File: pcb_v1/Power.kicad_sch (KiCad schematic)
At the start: 7 parts, among them J1 Conn_01x02, J2 Conn_01x04, U5 MCP73831-2-OT

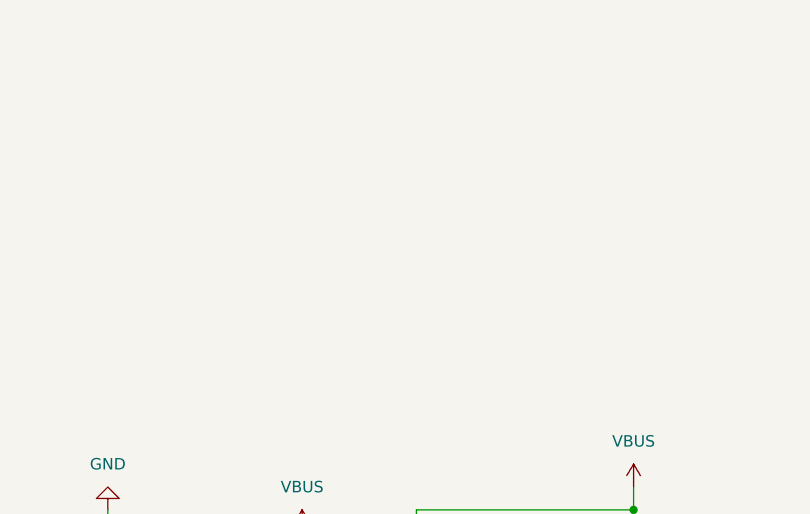
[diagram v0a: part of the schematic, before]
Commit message: New MCU. Added ESP32 S3 Mini1 to act as Bluetooth module
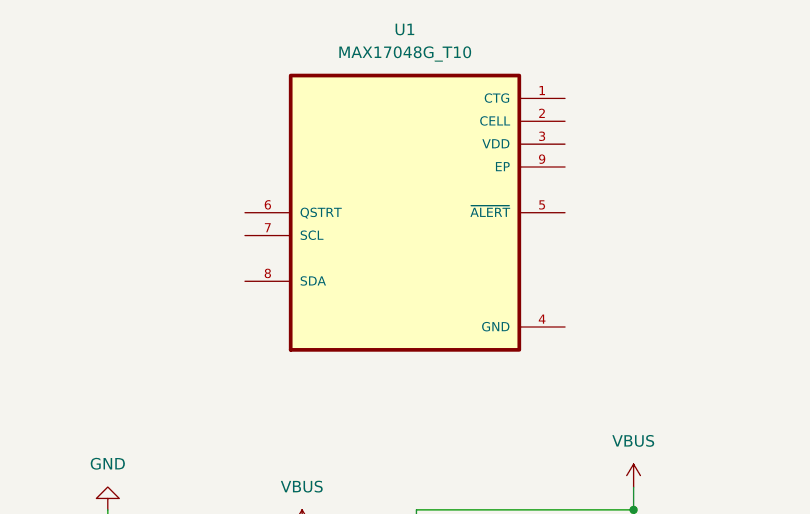
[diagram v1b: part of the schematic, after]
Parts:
- added U1: MAX17048G_T10, MAX17048G_T10:SON50P200X200X80-9N, symbol MAX17048G_T10:MAX17048G_T10
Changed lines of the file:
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@@
+	)
+	(symbol
+		(lib_id "MAX17048G_T10:MAX17048G_T10")
+		(at 125.73 52.07 0)
+		(unit 1)
+		(exclude_from_sim no)
+		(in_bom yes)
+		(on_board yes)
+		(dnp no)
+		(fields_autoplaced yes)
+		(property "Reference" "U1"
+			(at 125.73 31.75 0)
+			(effects
+				(font
+					(size 1.27 1.27)
+				)
+			)
+		)
+		(property "Value" "MAX17048G_T10"
+			(at 125.73 34.29 0)
+			(effects
+				(font
+					(size 1.27 1.27)
+				)
+			)
+		)
+		(property "Footprint" "MAX17048G_T10:SON50P200X200X80-9N"
+			(at 125.73 52.07 0)
+			(effects
+				(font
+					(size 1.27 1.27)
+				)
+				(justify bottom)
+				(hide yes)
+			)
+		)
+		(property "Datasheet" ""
+			(at 125.73 52.07 0)
+			(effects
+				(font
+					(size 1.27 1.27)
+				)
+				(hide yes)
+			)
+		)
+		(property "Description" ""
+			(at 125.73 52.07 0)
+			(effects
+				(font
+					(size 1.27 1.27)
+				)
+				(hide yes)
+			)
+		)
+		(property "MF" "Analog Devices"
+			(at 125.73 52.07 0)
+			(effects
+				(font
+					(size 1.27 1.27)
+				)
+				(justify bottom)
+				(hide yes)
+			)
+		)
+		(property "Description_1" "3µA 1-Cell/2-Cell Fuel Gauge with ModelGauge"
+			(at 125.73 52.07 0)
+			(effects
+				(font
+					(size 1.27 1.27)
+				)
+				(justify bottom)
+				(hide yes)
+			)
+		)
+		(property "Package" "TDFN-8 Maxim"
+			(at 125.73 52.07 0)
+			(effects
+				(font
+					(size 1.27 1.27)
+				)
+				(justify bottom)
+				(hide yes)
+			)
+		)
+		(property "Price" "None"
+			(at 125.73 52.07 0)
+			(effects
+				(font
+					(size 1.27 1.27)
+				)
+				(justify bottom)
+				(hide yes)
+			)
+		)
+		(property "SnapEDA_Link" "https://www.snapeda.com/parts/MAX17048G+T10/Analog+Devices/view-part/?ref=snap"
+			(at 125.73 52.07 0)
+			(effects
+				(font
+					(size 1.27 1.27)
+				)
+				(justify bottom)
+				(hide yes)
+			)
+		)
+		(property "MP" "MAX17048G+T10"
+			(at 125.73 52.07 0)
+			(effects
+				(font
+					(size 1.27 1.27)
+				)
+				(justify bottom)
+				(hide yes)
+			)
+		)
+		(property "Availability" "In Stock"
+			(at 125.73 52.07 0)
+			(effects
+				(font
+					(size 1.27 1.27)
+				)
+				(justify bottom)
+				(hide yes)
+			)
+		)
+		(property "Check_prices" "https://www.snapeda.com/parts/MAX17048G+T10/Analog+Devices/view-part/?ref=eda"
+			(at 125.73 52.07 0)
+			(effects
+				(font
+					(size 1.27 1.27)
+				)
+				(justify bottom)
+				(hide yes)
+			)
+		)
+		(pin "3"
+		)
+		(pin "9"
+		)
+		(pin "4"
+		)
+		(pin "2"
+		)
+		(pin "1"
+		)
+		(pin "6"
+		)
+		(pin "7"
+		)
+		(pin "5"
+		)
+		(pin "8"
+		)
+		(instances
+			(project ""
+				(path "/bf36a815-88b9-4f95-84c3-6b01513341e6/fa53453f-f231-4d4e-b453-0aed75af6d09"
+					(reference "U1")
+					(unit 1)
+				)
+			)
+		)
 	)
 	(symbol

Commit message: Updated wiring
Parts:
- C6, C7: footprint (none) -> Murata Capacitor:CAPC1608X90N
- R2, R4: footprint (none) -> Yageo Resistor:RESC1607X60N
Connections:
- net Status: no longer names the net of R2.2, U5.1 (STAT)
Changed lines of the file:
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@@
 		)
 	)
-	(global_label "Status"
+	(global_label "V_Battery"
 		(shape input)
-		(at 161.29 96.52 0)
+		(at 177.8 83.82 90)
 		(fields_autoplaced yes)
 		(effects
@@
 		)
 		(property "Intersheetrefs" "${INTERSHEET_REFS}"
-			(at 170.2622 96.52 0)
+			(at 177.8 72.0658 90)
 			(effects
 				(font
@@
 	(global_label "V_Battery"
 		(shape input)
-		(at 177.8 83.82 90)
+		(at 184.15 95.25 90)
 		(fields_autoplaced yes)
 		(effects
@@
 		)
 		(property "Intersheetrefs" "${INTERSHEET_REFS}"
-			(at 177.8 72.0658 90)
+			(at 184.15 83.4958 90)
 			(effects
 				(font
@@
 	(global_label "V_Battery"
 		(shape input)
-		(at 184.15 95.25 90)
+		(at 205.74 95.25 90)
 		(fields_autoplaced yes)
 		(effects
@@
 		)
 		(property "Intersheetrefs" "${INTERSHEET_REFS}"
-			(at 184.15 83.4958 90)
-			(effects
-				(font
-					(size 1.27 1.27)
-				)
-				(justify left)
-				(hide yes)
-			)
-		)
-	)
-	(global_label "V_Battery"
+			(at 205.74 83.4958 90)
+			(effects
+				(font
+					(size 1.27 1.27)
+				)
+				(justify left)
+				(hide yes)
+			)
+		)
+	)
+	(global_label "D-"
 		(shape input)
-		(at 205.74 95.25 90)
+		(at 92.71 92.71 0)
 		(fields_autoplaced yes)
 		(effects
@@
 		)
 		(property "Intersheetrefs" "${INTERSHEET_REFS}"
-			(at 205.74 83.4958 90)
-			(effects
-				(font
-					(size 1.27 1.27)
-				)
-				(justify left)
-				(hide yes)
-			)
-		)
-	)
-	(global_label "D-"
-		(shape input)
-		(at 92.71 92.71 0)
-		(fields_autoplaced yes)
-		(effects
-			(font
-				(size 1.27 1.27)
-			)
-			(justify left)
-		)
-		(property "Intersheetrefs" "${INTERSHEET_REFS}"
 			(at 98.5376 92.71 0)
 			(effects
@@
 			)
 		)
-		(property "Footprint" ""
+		(property "Footprint" "Murata Capacitor:CAPC1608X90N"
 			(at 115.2652 96.52 0)
 			(effects
@@
 			)
 		)
-		(property "Footprint" ""
+		(property "Footprint" "Yageo Resistor:RESC1607X60N"
 			(at 125.222 97.79 90)
 			(effects
@@
 			)
 		)
-		(property "Footprint" ""
+		(property "Footprint" "Murata Capacitor:CAPC1608X90N"
 			(at 185.1152 104.14 0)
 			(effects
@@
 			)
 		)
-		(property "Footprint" ""
+		(property "Footprint" "Yageo Resistor:RESC1607X60N"
 			(at 134.112 100.33 90)
 			(effects

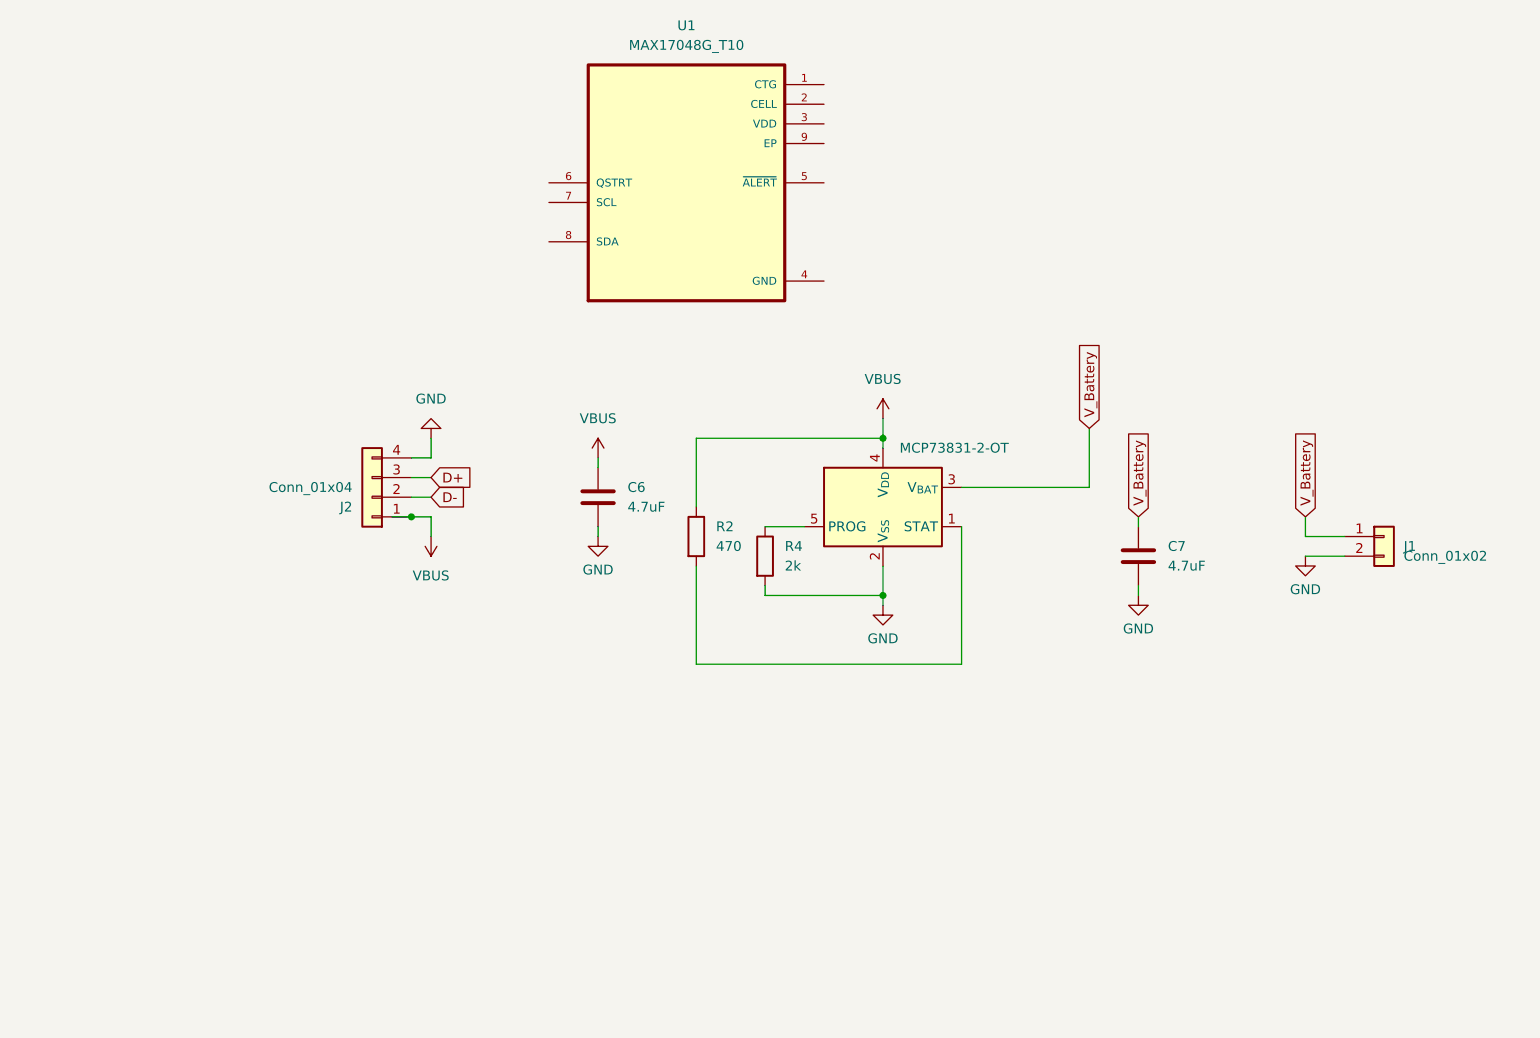
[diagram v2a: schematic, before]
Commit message: Connected OLED pin connector
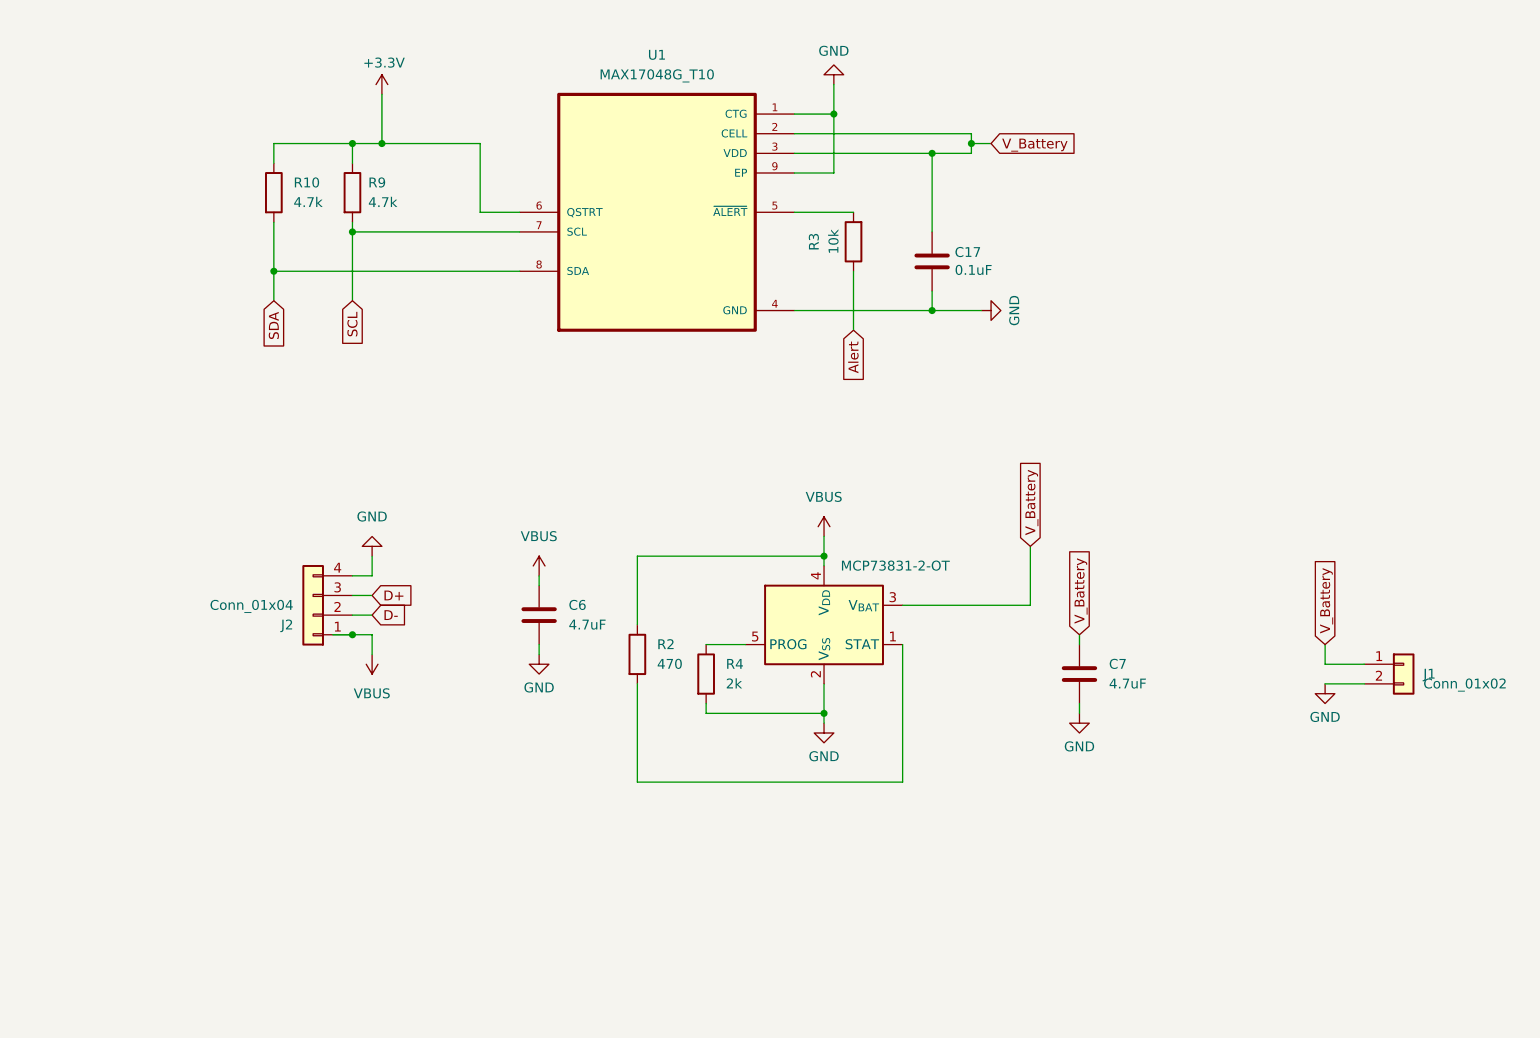
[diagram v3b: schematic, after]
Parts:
- added C17: 0.1uF, GRM1555C2A101GA01D:CAPC1005X55N, symbol Device:C
- added R10, R9: 4.7k, RC0402FR-7D4K7L:RESC1005X40N, symbol Device:R
- added R3: 10k, RC0402FR-7D4K7L:RESC1005X40N, symbol ScottoKeebs:Placeholder_Resistor
- C6, C7: footprint Murata Capacitor:CAPC1608X90N -> GRM1555C2A101GA01D:CAPC1005X55N
- R2, R4: footprint Yageo Resistor:RESC1607X60N -> RC0402FR-7D4K7L:RESC1005X40N
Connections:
- net GND: now also U1.1 (CTG), U1.4 (GND), U1.9 (EP), C17.2
- net V_Battery: now also U1.2 (CELL), U1.3 (VDD), C17.1
- net at U1.5 (~{ALERT}): now also R3.2
- net +3.3V: now reaches U1.6 (QSTRT)
- net +3.3V: now also R10.1, R9.1
- net SCL: now reaches U1.7 (SCL)
- net SCL: now also R9.2
- net SDA: now reaches U1.8 (SDA)
- net SDA: now also R10.2
- new net Alert: R3.1
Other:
- moved on the sheet: C6, C7, J1, J2, R2, R4, U1

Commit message: New Charger IC, Added Ground Plane
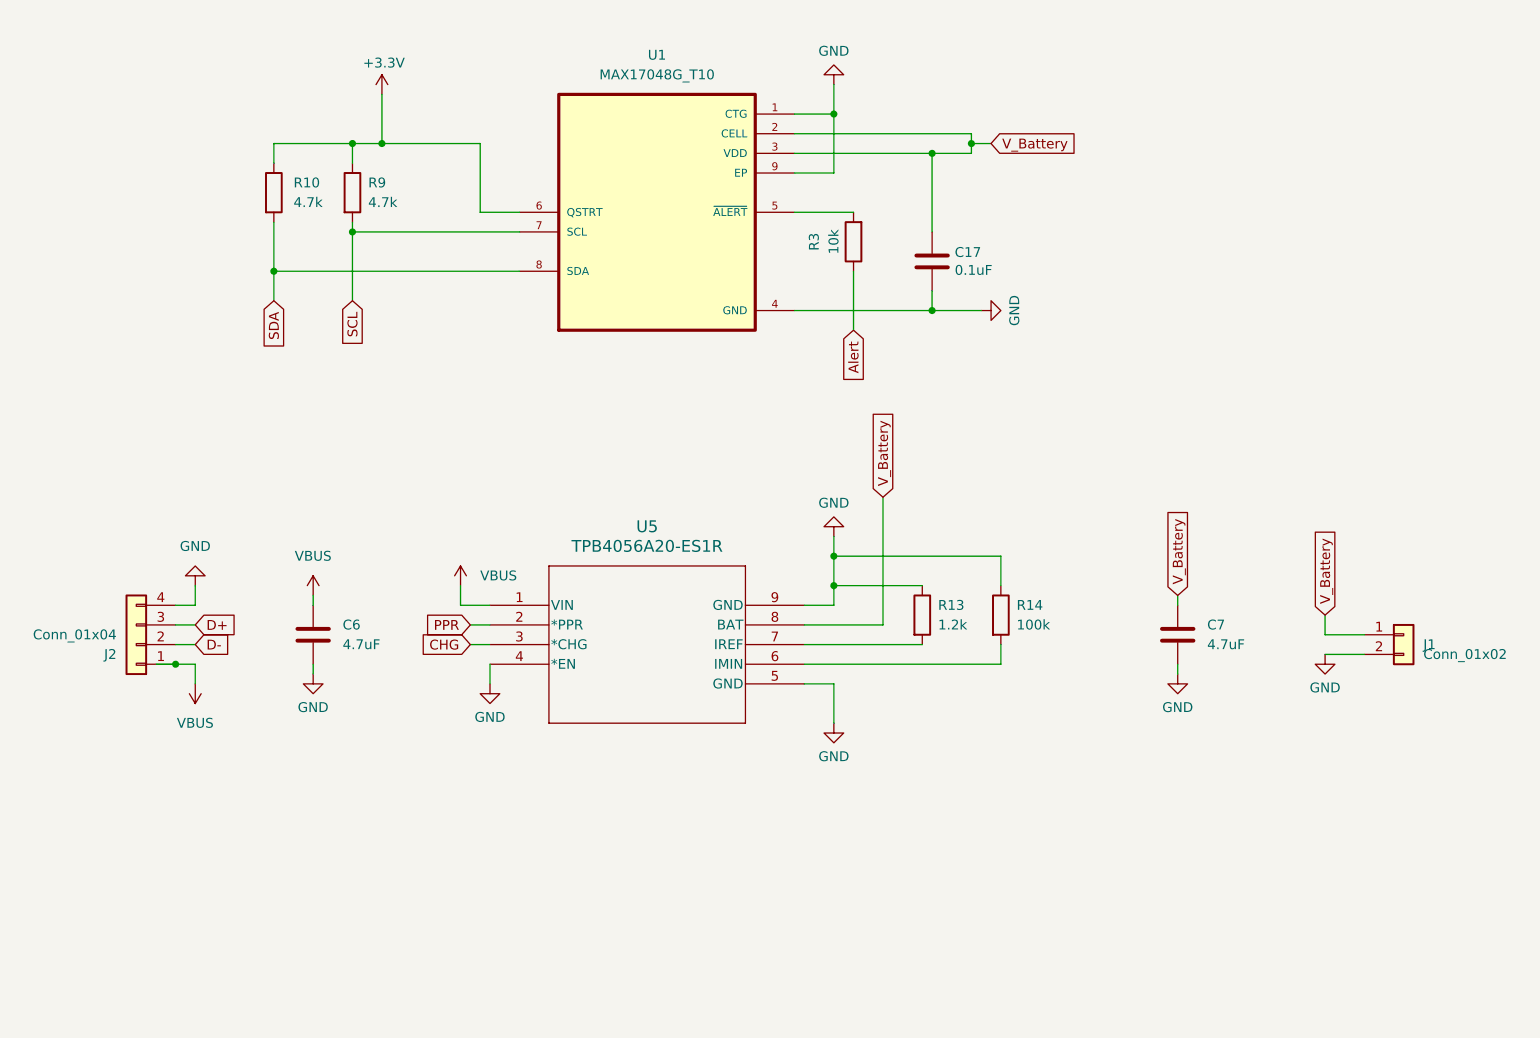
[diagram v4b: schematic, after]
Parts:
- removed R2: 470, RC0402FR-7D4K7L:RESC1005X40N, symbol Device:R
- removed R4: 2k, RC0402FR-7D4K7L:RESC1005X40N, symbol Device:R
- removed U5: MCP73831-2-OT, Package_TO_SOT_SMD:SOT-23-5, symbol Battery_Management:MCP73831-2-OT
- added R13: 1.2k, RC0402FR-7D4K7L:RESC1005X40N, symbol Device:R
- added R14: 100k, RC0402FR-7D4K7L:RESC1005X40N, symbol Device:R
- added U5: TPB4056A20-ES1R, TPB4056A20_ES1R:ESOP-8_TPK, symbol 2025-05-27_22-00-58:TPB4056A20-ES1R
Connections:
- net GND: now also R13.1, R14.1, U5.4 (*EN), U5.5 (GND), U5.9 (GND)
- net VBUS: now also U5.1 (VIN)
- net V_Battery: now also U5.8 (BAT)
- new net: R14.2, U5.6 (IMIN)
- new net: R13.2, U5.7 (IREF)
- new net CHG: U5.3 (*CHG)
- new net PPR: U5.2 (*PPR)
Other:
- moved on the sheet: C6, C7, J1, J2

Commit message: Updated thru holes and connector sizings
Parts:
- J1: footprint Connector_JST:JST_SH_SM02B-SRSS-TB_1x02-1MP_P1.00mm_Horizontal -> Connector_JST:JST_PH_S2B-PH-SM4-TB_1x02-1MP_P2.00mm_Horizontal
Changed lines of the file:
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@@
 			)
 		)
-		(property "Footprint" "Connector_JST:JST_SH_SM02B-SRSS-TB_1x02-1MP_P1.00mm_Horizontal"
+		(property "Footprint" "Connector_JST:JST_PH_S2B-PH-SM4-TB_1x02-1MP_P2.00mm_Horizontal"
 			(at 218.44 110.49 0)
 			(effects
